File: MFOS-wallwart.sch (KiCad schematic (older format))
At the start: 31 parts, among them J1 Barrel_Jack, J2 Connector_Generic:Conn_02x08_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, J3 Conn_02x05_Odd_Even, SW1 SW_SPST, U1 L7812, U2 L7912, U3 L7805

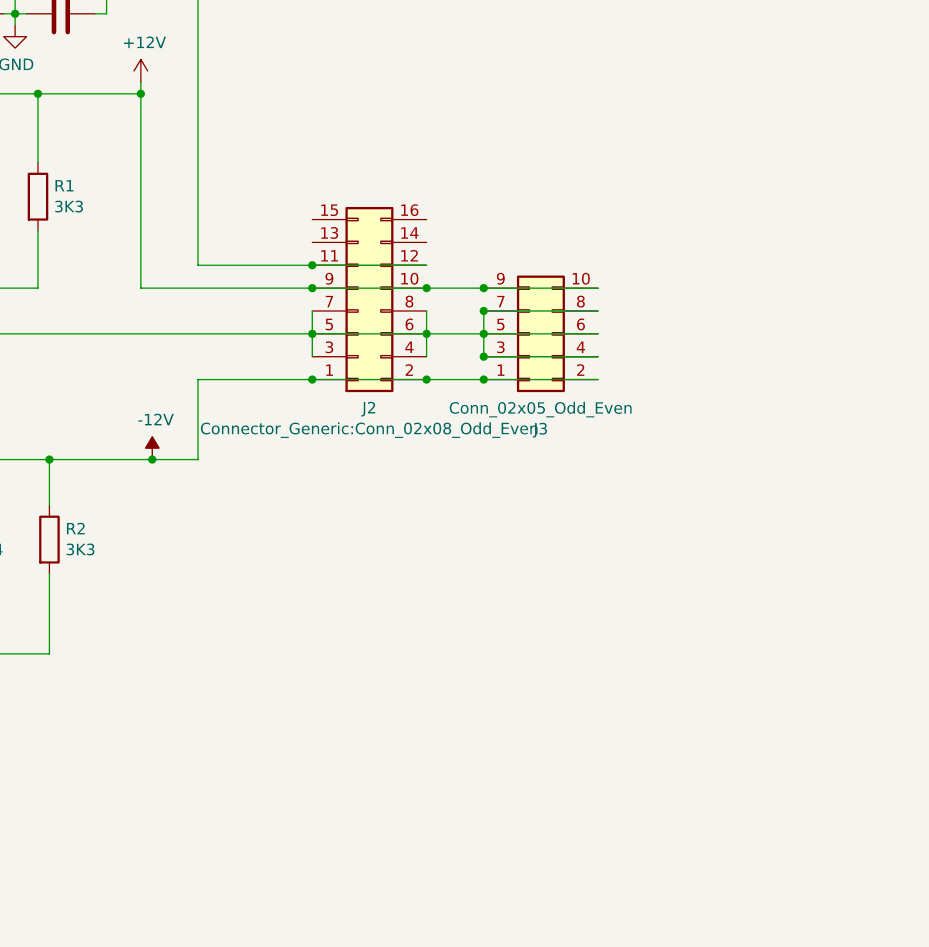
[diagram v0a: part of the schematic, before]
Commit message: Updated for extra outputs
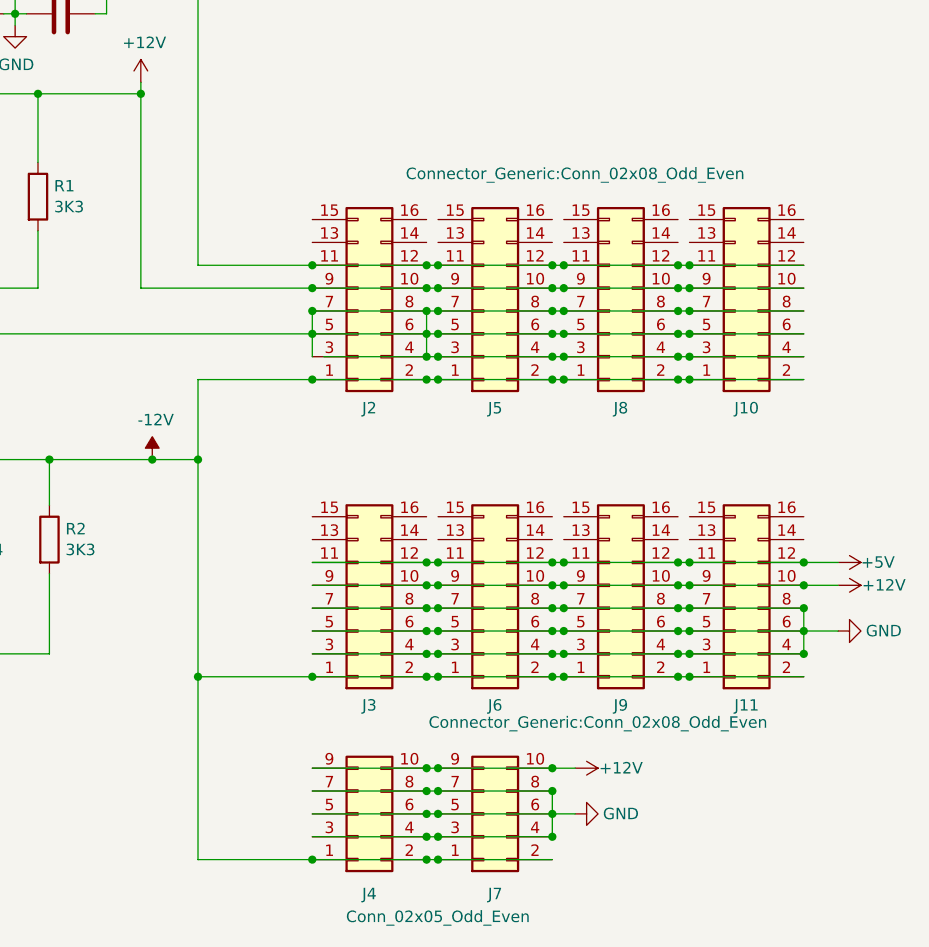
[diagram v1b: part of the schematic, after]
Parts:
- removed J3: Conn_02x05_Odd_Even, Connector_PinHeader_2.54mm:PinHeader_2x05_P2.54mm_Vertical, symbol Connector_Generic:Conn_02x05_Odd_Even
- added J10, J11, J3, J5, J6, J8, J9: Connector_Generic:Conn_02x08_Odd_Even, Connector_IDC:IDC-Header_2x08_P2.54mm_Vertical, symbol Connector_Generic:Conn_02x08_Odd_Even
- added J4, J7: Conn_02x05_Odd_Even, Connector_PinHeader_2.54mm:PinHeader_2x05_P2.54mm_Vertical, symbol Connector_Generic:Conn_02x05_Odd_Even
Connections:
- net +12V: now also J10.10 (Pin_10), J10.9 (Pin_9), J11.10 (Pin_10), J11.9 (Pin_9), J3.10 (Pin_10), J3.9 (Pin_9), J4.10 (Pin_10), J4.9 (Pin_9), J5.10 (Pin_10), J5.9 (Pin_9), J6.10 (Pin_10), J6.9 (Pin_9), J7.10 (Pin_10), J7.9 (Pin_9), J8.10 (Pin_10), J8.9 (Pin_9), J9.10 (Pin_10), J9.9 (Pin_9)
- net +5V: now also J10.11 (Pin_11), J10.12 (Pin_12), J11.11 (Pin_11), J11.12 (Pin_12), J3.11 (Pin_11), J3.12 (Pin_12), J5.11 (Pin_11), J5.12 (Pin_12), J6.11 (Pin_11), J6.12 (Pin_12), J8.11 (Pin_11), J8.12 (Pin_12), J9.11 (Pin_11), J9.12 (Pin_12)
- net -12V: now also J10.1 (Pin_1), J10.2 (Pin_2), J11.1 (Pin_1), J11.2 (Pin_2), J3.1 (Pin_1), J3.2 (Pin_2), J4.1 (Pin_1), J4.2 (Pin_2), J5.1 (Pin_1), J5.2 (Pin_2), J6.1 (Pin_1), J6.2 (Pin_2), J7.1 (Pin_1), J7.2 (Pin_2), J8.1 (Pin_1), J8.2 (Pin_2), J9.1 (Pin_1), J9.2 (Pin_2)
- net GND: now also J10.3 (Pin_3), J10.4 (Pin_4), J10.5 (Pin_5), J10.6 (Pin_6), J10.7 (Pin_7), J10.8 (Pin_8), J11.3 (Pin_3), J11.4 (Pin_4), J11.5 (Pin_5), J11.6 (Pin_6), J11.7 (Pin_7), J11.8 (Pin_8), J3.3 (Pin_3), J3.4 (Pin_4), J3.5 (Pin_5), J3.6 (Pin_6), J3.7 (Pin_7), J3.8 (Pin_8), J4.3 (Pin_3), J4.4 (Pin_4), J4.5 (Pin_5), J4.6 (Pin_6), J4.7 (Pin_7), J4.8 (Pin_8), J5.3 (Pin_3), J5.4 (Pin_4), J5.5 (Pin_5), J5.6 (Pin_6), J5.7 (Pin_7), J5.8 (Pin_8), J6.3 (Pin_3), J6.4 (Pin_4), J6.5 (Pin_5), J6.6 (Pin_6), J6.7 (Pin_7), J6.8 (Pin_8), J7.3 (Pin_3), J7.4 (Pin_4), J7.5 (Pin_5), J7.6 (Pin_6), J7.7 (Pin_7), J7.8 (Pin_8), J8.3 (Pin_3), J8.4 (Pin_4), J8.5 (Pin_5), J8.6 (Pin_6), J8.7 (Pin_7), J8.8 (Pin_8), J9.3 (Pin_3), J9.4 (Pin_4), J9.5 (Pin_5), J9.6 (Pin_6), J9.7 (Pin_7), J9.8 (Pin_8)

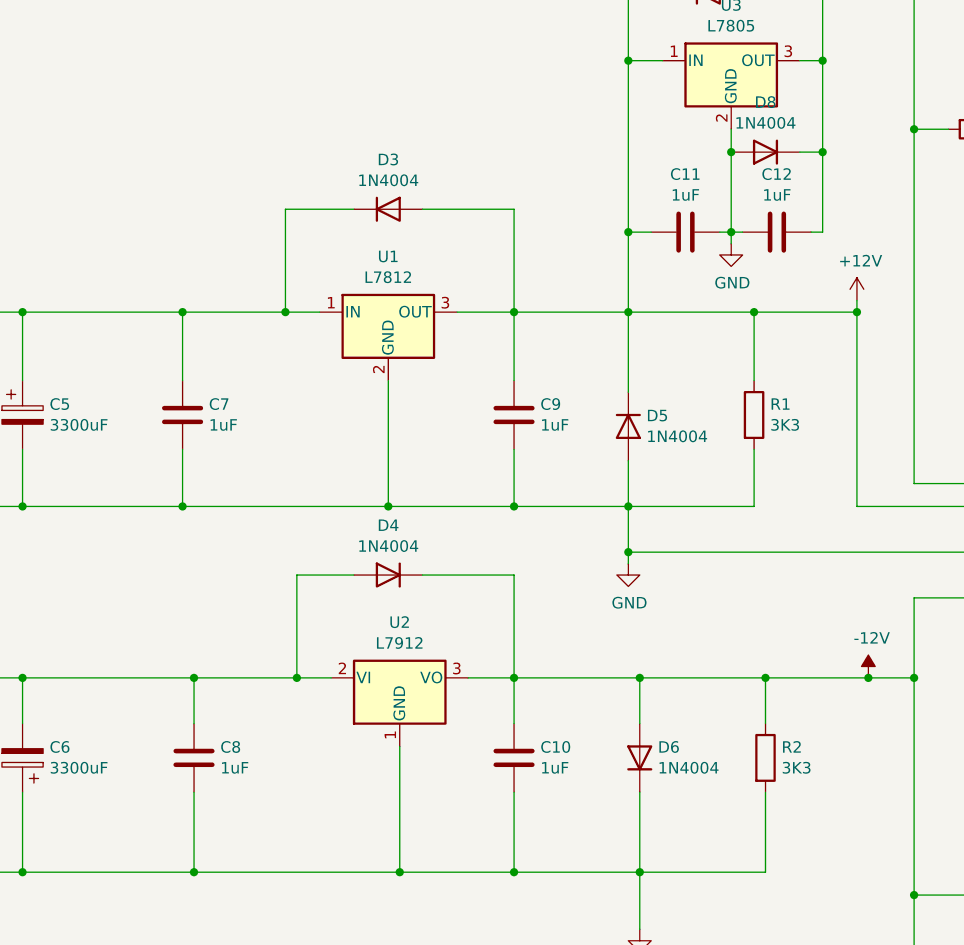
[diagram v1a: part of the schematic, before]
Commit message: Minor updates, add polarity to 1uf caps
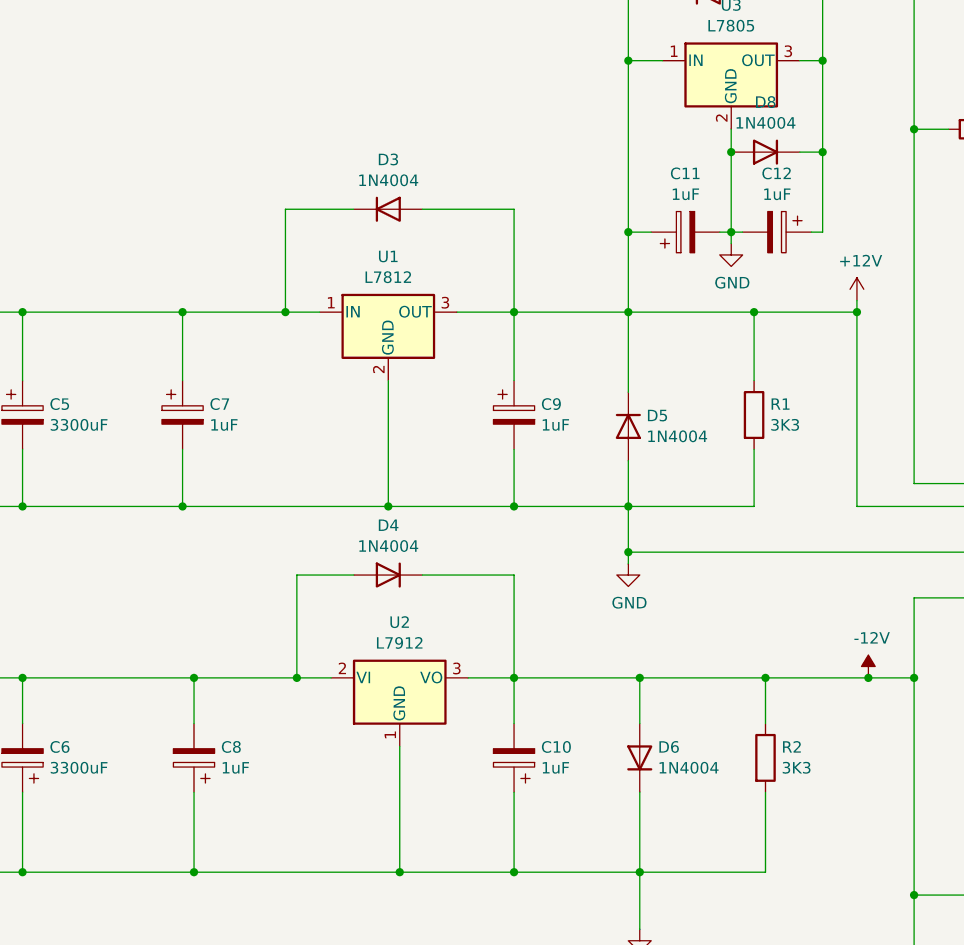
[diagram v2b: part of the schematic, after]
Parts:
- removed C10, C11, C12, C7, C8, C9: 1uF, Capacitor_THT:C_Radial_D6.3mm_H5.0mm_P2.50mm, symbol Device:C
- added C10, C11, C12, C7, C8, C9: 1uF, Capacitor_THT:CP_Radial_D6.3mm_P2.50mm, symbol Device:CP
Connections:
- net +12V: now also C11.1, C9.1
- net +5V: now also C12.1
- net -12V: now also C10.2
- net GND: now also C10.1, C11.2, C12.2, C7.2, C8.1, C9.2
- net at C1.1, C3.1, C5.1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: now also C7.1
- net at C2.2, C4.2, C6.2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: now also C8.2
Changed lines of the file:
@@
 	1    0    0    1
-$EndComp
-$Comp
-L Device:C C7
-U 1 1 5F265251
-P 4600 3000
-F 0 "C7" H 4715 3046 50  0000 L CNN
-F 1 "1uF" H 4715 2955 50  0000 L CNN
-F 2 "Capacitor_THT:C_Radial_D6.3mm_H5.0mm_P2.50mm" H 4638 2850 50  0001 C CNN
-F 3 "~" H 4600 3000 50  0001 C CNN
-	1    4600 3000
-	1    0    0    -1
-$EndComp
-$Comp
-L Device:C C8
-U 1 1 5F26694C
-P 4650 4500
-F 0 "C8" H 4765 4546 50  0000 L CNN
-F 1 "1uF" H 4765 4455 50  0000 L CNN
-F 2 "Capacitor_THT:C_Radial_D6.3mm_H5.0mm_P2.50mm" H 4688 4350 50  0001 C CNN
-F 3 "~" H 4650 4500 50  0001 C CNN
-	1    4650 4500
-	1    0    0    -1
-$EndComp
-$Comp
-L Device:C C9
-U 1 1 5F266C0B
-P 6050 3000
-F 0 "C9" H 6165 3046 50  0000 L CNN
-F 1 "1uF" H 6165 2955 50  0000 L CNN
-F 2 "Capacitor_THT:C_Radial_D6.3mm_H5.0mm_P2.50mm" H 6088 2850 50  0001 C CNN
-F 3 "~" H 6050 3000 50  0001 C CNN
-	1    6050 3000
-	1    0    0    -1
 $EndComp
 Wire Wire Line
@@
 	5500 3400 4600 3400
 Wire Wire Line
-	4650 4350 4650 4150
-Wire Wire Line
 	4650 4150 5100 4150
 Wire Wire Line
@@
 	5550 4450 5550 5000
 Connection ~ 5550 5000
-Wire Wire Line
-	4650 4650 4650 5000
 Connection ~ 4650 5000
 Wire Wire Line
@@
 Wire Wire Line
 	6600 4150 6600 4350
-$Comp
-L Device:C C10
-U 1 1 5F266FE5
-P 6050 4500
-F 0 "C10" H 6165 4546 50  0000 L CNN
-F 1 "1uF" H 6165 4455 50  0000 L CNN
-F 2 "Capacitor_THT:C_Radial_D6.3mm_H5.0mm_P2.50mm" H 6088 4350 50  0001 C CNN
-F 3 "~" H 6050 4500 50  0001 C CNN
-	1    6050 4500
-	1    0    0    -1
-$EndComp
 $Comp
 L Diode:1N4004 D6
@@
 	-1   0    0    1
 $EndComp
-$Comp
-L Device:C C11
-U 1 1 60205FC3
-P 6800 2200
-F 0 "C11" V 6548 2200 50  0000 C CNN
-F 1 "1uF" V 6639 2200 50  0000 C CNN
-F 2 "Capacitor_THT:C_Radial_D6.3mm_H5.0mm_P2.50mm" H 6838 2050 50  0001 C CNN
-F 3 "~" H 6800 2200 50  0001 C CNN
-	1    6800 2200
-	0    1    1    0
-$EndComp
-$Comp
-L Device:C C12
-U 1 1 60217119
-P 7200 2200
-F 0 "C12" V 6948 2200 50  0000 C CNN
-F 1 "1uF" V 7039 2200 50  0000 C CNN
-F 2 "Capacitor_THT:C_Radial_D6.3mm_H5.0mm_P2.50mm" H 7238 2050 50  0001 C CNN
-F 3 "~" H 7200 2200 50  0001 C CNN
-	1    7200 2200
-	0    1    1    0
-$EndComp
 Wire Wire Line
 	6550 1150 6550 1450
@@
 	7950 1750 7800 1750
 Connection ~ 7800 1750
-Wire Wire Line
-	7800 1750 7800 3300
 $Comp
 L Connector_Generic:Conn_02x08_Odd_Even J5
@@
 Wire Wire Line
 	8300 5100 7800 5100
+$Comp
+L Device:CP C7
+U 1 1 60563132
+P 4600 3000
+F 0 "C7" H 4718 3046 50  0000 L CNN
+F 1 "1uF" H 4718 2955 50  0000 L CNN
+F 2 "Capacitor_THT:CP_Radial_D6.3mm_P2.50mm" H 4638 2850 50  0001 C CNN
+F 3 "~" H 4600 3000 50  0001 C CNN
+	1    4600 3000
+	1    0    0    -1
+$EndComp
+$Comp
+L Device:CP C8
+U 1 1 6057A7D5
+P 4650 4500
+F 0 "C8" H 4532 4454 50  0000 R CNN
+F 1 "1uF" H 4532 4545 50  0000 R CNN
+F 2 "Capacitor_THT:CP_Radial_D6.3mm_P2.50mm" H 4688 4350 50  0001 C CNN
+F 3 "~" H 4650 4500 50  0001 C CNN
+	1    4650 4500
+	-1   0    0    1
+$EndComp
+Wire Wire Line
+	4650 4650 4650 5000
+Wire Wire Line
+	4650 4150 4650 4350
+$Comp
+L Device:CP C9
+U 1 1 6059338F
+P 6050 3000
+F 0 "C9" H 6168 3046 50  0000 L CNN
+F 1 "1uF" H 6168 2955 50  0000 L CNN
+F 2 "Capacitor_THT:CP_Radial_D6.3mm_P2.50mm" H 6088 2850 50  0001 C CNN
+F 3 "~" H 6050 3000 50  0001 C CNN
+	1    6050 3000
+	1    0    0    -1
+$EndComp
+$Comp
+L Device:CP C10
+U 1 1 605B1749
+P 6050 4500
+F 0 "C10" H 5932 4454 50  0000 R CNN
+F 1 "1uF" H 5932 4545 50  0000 R CNN
+F 2 "Capacitor_THT:CP_Radial_D6.3mm_P2.50mm" H 6088 4350 50  0001 C CNN
+F 3 "~" H 6050 4500 50  0001 C CNN
+	1    6050 4500
+	-1   0    0    1
+$EndComp
+$Comp
+L Device:CP C11
+U 1 1 605C379C
+P 6800 2200
+F 0 "C11" V 7055 2200 50  0000 C CNN
+F 1 "1uF" V 6964 2200 50  0000 C CNN
+F 2 "Capacitor_THT:CP_Radial_D6.3mm_P2.50mm" H 6838 2050 50  0001 C CNN
+F 3 "~" H 6800 2200 50  0001 C CNN
+	1    6800 2200
+	0    -1   -1   0
+$EndComp
+$Comp
+L Device:CP C12
+U 1 1 605C543E
+P 7200 2200
+F 0 "C12" V 6945 2200 50  0000 C CNN
+F 1 "1uF" V 7036 2200 50  0000 C CNN
+F 2 "Capacitor_THT:CP_Radial_D6.3mm_P2.50mm" H 7238 2050 50  0001 C CNN
+F 3 "~" H 7200 2200 50  0001 C CNN
+	1    7200 2200
+	0    1    1    0
+$EndComp
+Wire Wire Line
+	7800 1750 7800 3300
 $EndSCHEMATC
